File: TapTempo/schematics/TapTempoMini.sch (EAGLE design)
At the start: 57 parts, among them IC3 TL072D, Q2 8MHz, Q301 BC846, Q701 BC846, U1 STM32F100CBT6B, U3 NCP702

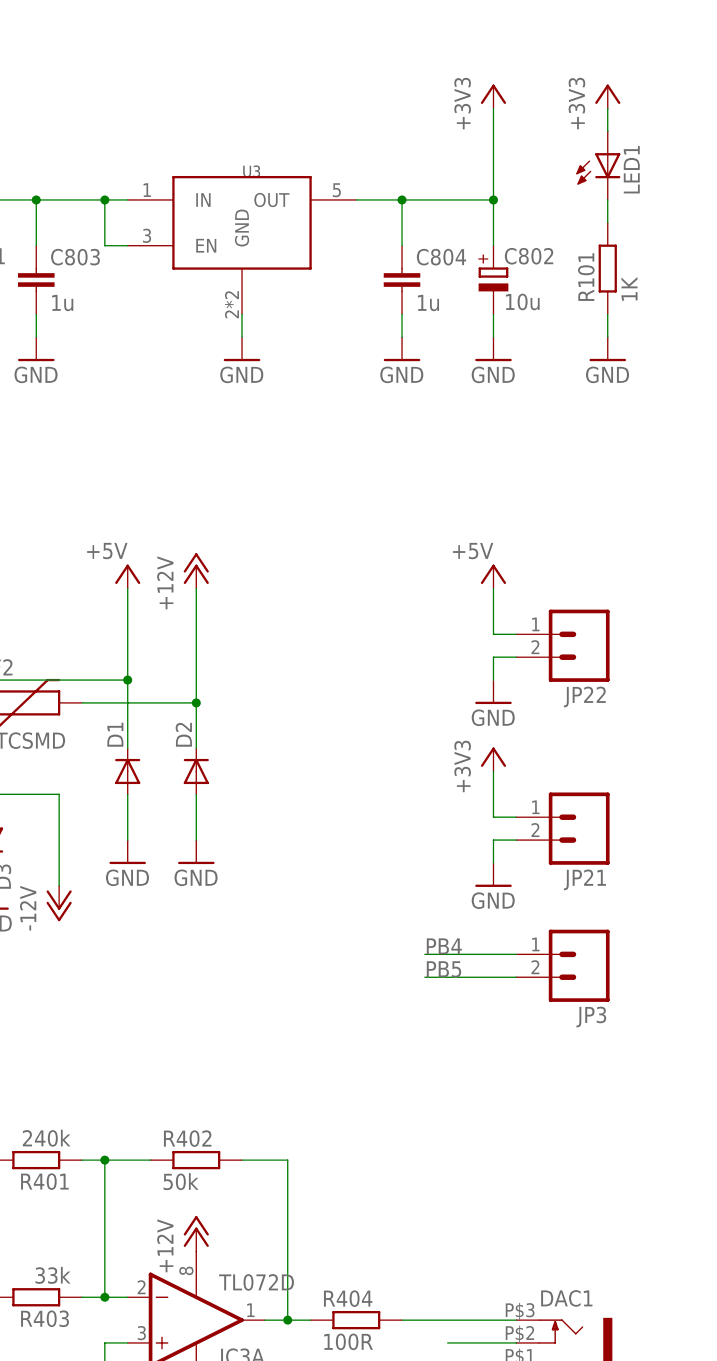
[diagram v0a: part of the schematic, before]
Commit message: removed led and changed 50k R402 to standard value 51k
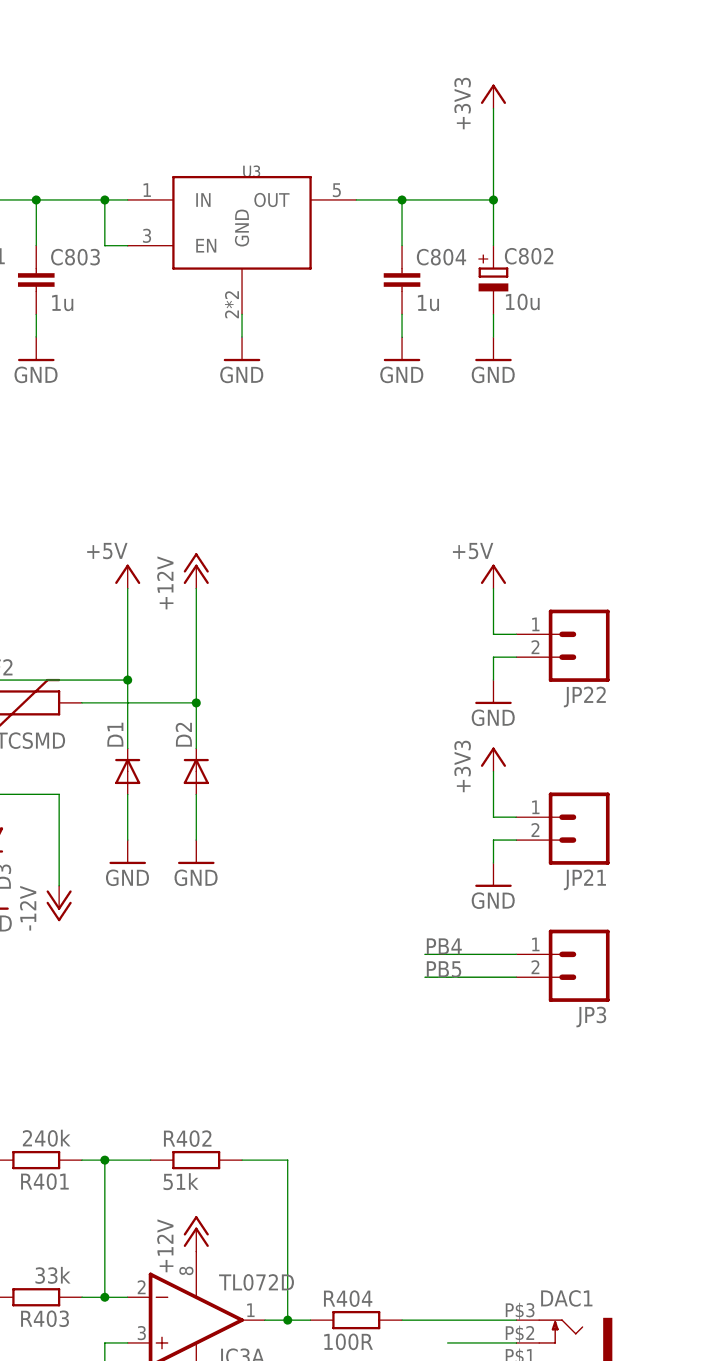
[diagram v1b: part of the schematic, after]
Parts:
- removed LED1: (no value), led:LEDCHIPLED_0603
- removed R101: 1K, resistor:R-EU_R0603
- R402: value 50k -> 51k
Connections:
- removed net N$19: LED1.C, R101.2
- net +3V3: no longer LED1.A
- net GND: no longer R101.1
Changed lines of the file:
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@@
 <part name="DAC1" library="Rebel" deviceset="THONKICONN" device=""/>
 <part name="R401" library="resistor" deviceset="R-EU_" device="R0603" value="240k"/>
-<part name="R402" library="resistor" deviceset="R-EU_" device="R0603" value="50k"/>
+<part name="R402" library="resistor" deviceset="R-EU_" device="R0603" value="51k"/>
 <part name="GND6" library="supply1" deviceset="GND" device=""/>
 <part name="+3V2" library="supply1" deviceset="+3V3" device=""/>
@@
 <part name="GND41" library="supply1" deviceset="GND" device=""/>
 <part name="GND42" library="supply1" deviceset="GND" device=""/>
-<part name="LED1" library="led" deviceset="LED" device="CHIPLED_0603"/>
-<part name="R101" library="resistor" deviceset="R-EU_" device="R0603" value="1K"/>
-<part name="+3V19" library="supply1" deviceset="+3V3" device=""/>
-<part name="GND23" library="supply1" deviceset="GND" device=""/>
 <part name="GND59" library="supply1" deviceset="GND" device=""/>
 <part name="R100" library="Rebel" deviceset="R-EU_" device="0603" value="150R"/>
@@
 <instance part="GND41" gate="1" x="190.5" y="88.9"/>
 <instance part="GND42" gate="1" x="190.5" y="109.22"/>
-<instance part="LED1" gate="G$1" x="203.2" y="170.18"/>
-<instance part="R101" gate="G$1" x="203.2" y="157.48" rot="R90"/>
-<instance part="+3V19" gate="G$1" x="203.2" y="177.8"/>
-<instance part="GND23" gate="1" x="203.2" y="147.32"/>
 <instance part="GND59" gate="1" x="-7.62" y="-20.32"/>
 <instance part="R100" gate="G$1" x="81.28" y="177.8" rot="R180"/>
@@
 </segment>
 <segment>
-<pinref part="GND23" gate="1" pin="GND"/>
-<pinref part="R101" gate="G$1" pin="1"/>
-<wire x1="203.2" y1="149.86" x2="203.2" y2="152.4" width="0.1524" layer="91"/>
-</segment>
-<segment>
 <pinref part="PULSE" gate="G$1" pin="5"/>
 <pinref part="GND46" gate="1" pin="GND"/>
@@
 <wire x1="193.04" y1="96.52" x2="190.5" y2="96.52" width="0.1524" layer="91"/>
 <wire x1="190.5" y1="96.52" x2="190.5" y2="101.6" width="0.1524" layer="91"/>
-</segment>
-<segment>
-<pinref part="LED1" gate="G$1" pin="A"/>
-<pinref part="+3V19" gate="G$1" pin="+3V3"/>
-<wire x1="203.2" y1="172.72" x2="203.2" y2="175.26" width="0.1524" layer="91"/>
 </segment>
 <segment>
@@
 </segment>
 </net>
-<net name="N$19" class="0">
-<segment>
-<pinref part="R101" gate="G$1" pin="2"/>
-<pinref part="LED1" gate="G$1" pin="C"/>
-<wire x1="203.2" y1="162.56" x2="203.2" y2="165.1" width="0.1524" layer="91"/>
-</segment>
-</net>

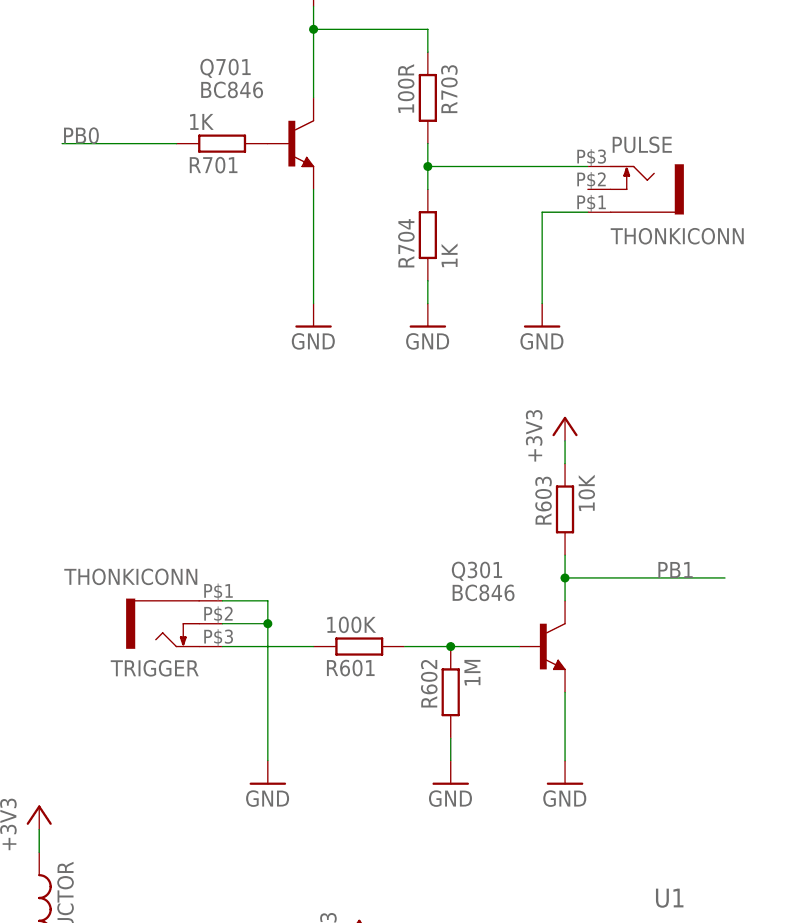
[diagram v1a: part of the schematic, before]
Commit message: normalled trigger input to pulse output
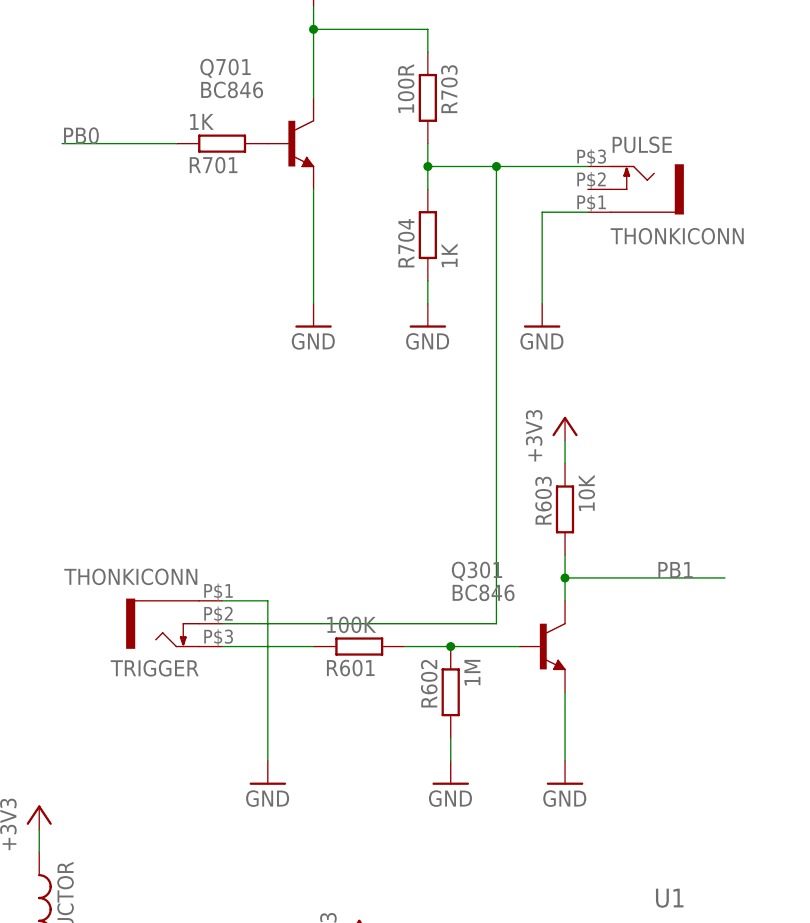
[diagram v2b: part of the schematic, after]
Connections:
- net GND: no longer TRIGGER.4
- net N$35: now also TRIGGER.4
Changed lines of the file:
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@@
 <pinref part="GND29" gate="1" pin="GND"/>
 <pinref part="TRIGGER" gate="G$1" pin="5"/>
-<wire x1="-17.78" y1="101.6" x2="-17.78" y2="99.06" width="0.1524" layer="91"/>
-<pinref part="TRIGGER" gate="G$1" pin="4"/>
-<wire x1="-17.78" y1="99.06" x2="-17.78" y2="83.82" width="0.1524" layer="91"/>
-<wire x1="-22.86" y1="99.06" x2="-17.78" y2="99.06" width="0.1524" layer="91"/>
-<junction x="-17.78" y="99.06"/>
+<wire x1="-17.78" y1="101.6" x2="-17.78" y2="83.82" width="0.1524" layer="91"/>
 </segment>
 <segment>
@@
 <wire x1="0" y1="152.4" x2="0" y2="149.86" width="0.1524" layer="91"/>
 <wire x1="0" y1="149.86" x2="0" y2="147.32" width="0.1524" layer="91"/>
-<wire x1="0" y1="149.86" x2="17.78" y2="149.86" width="0.1524" layer="91"/>
+<wire x1="0" y1="149.86" x2="7.62" y2="149.86" width="0.1524" layer="91"/>
 <junction x="0" y="149.86"/>
 <pinref part="PULSE" gate="G$1" pin="3"/>
-</segment>
-</net>
+<pinref part="TRIGGER" gate="G$1" pin="4"/>
+<wire x1="7.62" y1="149.86" x2="17.78" y2="149.86" width="0.1524" layer="91"/>
+<wire x1="-22.86" y1="99.06" x2="7.62" y2="99.06" width="0.1524" layer="91"/>
+<wire x1="7.62" y1="99.06" x2="7.62" y2="149.86" width="0.1524" layer="91"/>
+<junction x="7.62" y="149.86"/>
+</segment>
+</net>

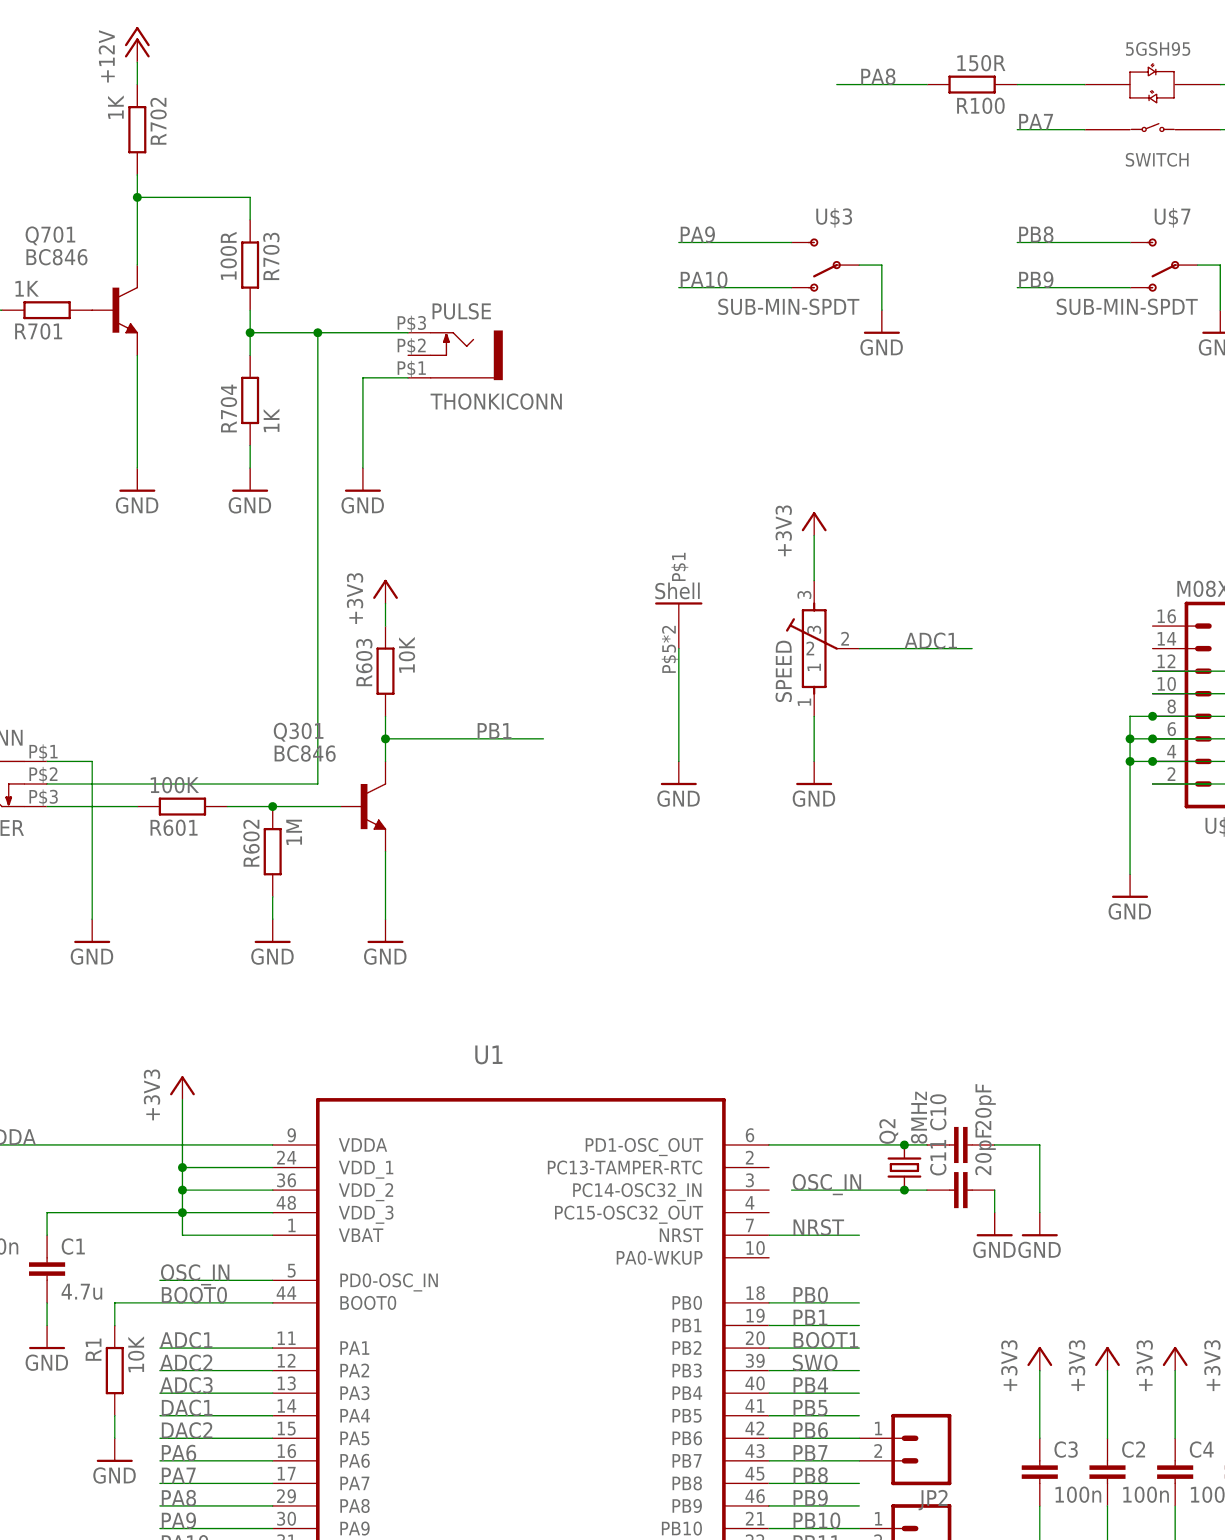
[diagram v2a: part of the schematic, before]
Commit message: swapped pot and pushbutton, rerouted, changed thonkiconn footprint to 1mm holes
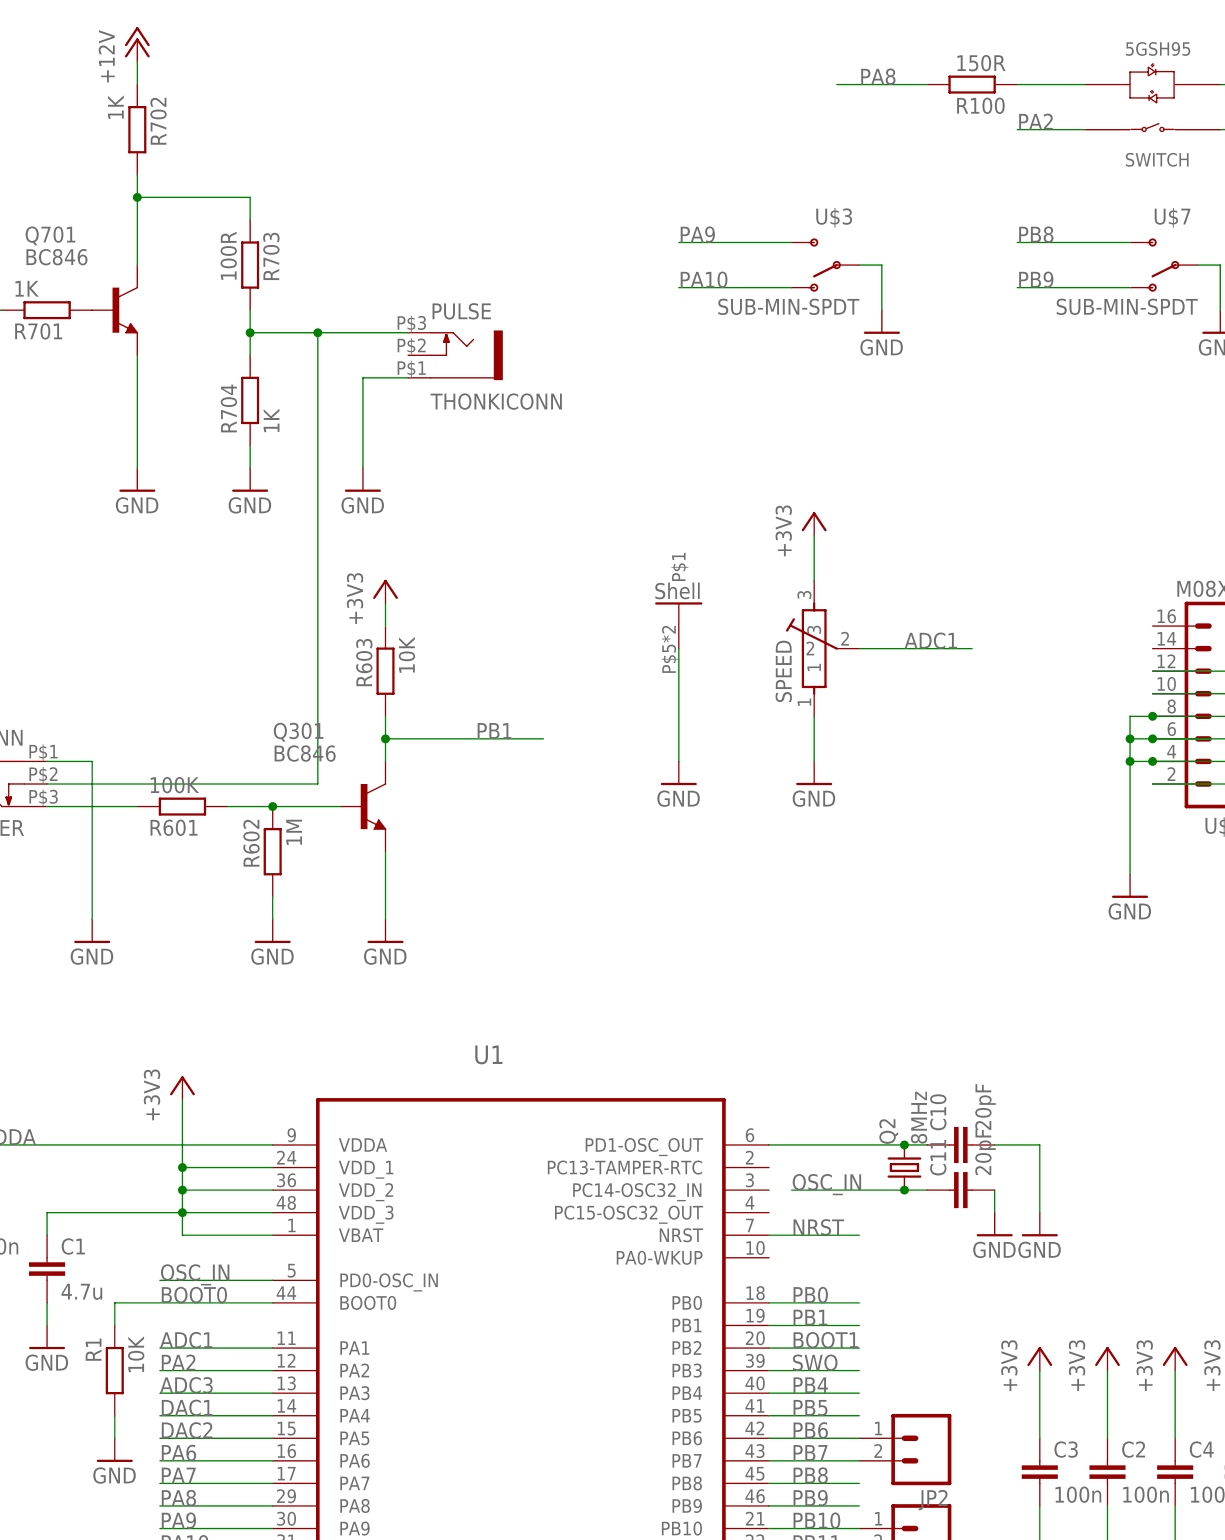
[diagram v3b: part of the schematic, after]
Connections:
- removed net ADC2: U1.PA2
- new net PA2: U$1.SWITCH_A, U1.PA2
- net PA7: no longer U$1.SWITCH_A
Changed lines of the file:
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@@
 </segment>
 </net>
-<net name="ADC2" class="0">
+<net name="PA2" class="0">
 <segment>
 <pinref part="U1" gate="A" pin="PA2"/>
 <wire x1="2.54" y1="33.02" x2="-10.16" y2="33.02" width="0.1524" layer="91"/>
 <label x="-10.16" y="33.02" size="1.778" layer="95"/>
+</segment>
+<segment>
+<pinref part="U$1" gate="G$1" pin="SWITCH_A"/>
+<wire x1="93.98" y1="172.72" x2="86.36" y2="172.72" width="0.1524" layer="91"/>
+<label x="86.36" y="172.72" size="1.778" layer="95"/>
 </segment>
 </net>
@@
 <label x="-10.16" y="20.32" size="1.778" layer="95"/>
 </segment>
-<segment>
-<pinref part="U$1" gate="G$1" pin="SWITCH_A"/>
-<wire x1="93.98" y1="172.72" x2="86.36" y2="172.72" width="0.1524" layer="91"/>
-<label x="86.36" y="172.72" size="1.778" layer="95"/>
-</segment>
 </net>
